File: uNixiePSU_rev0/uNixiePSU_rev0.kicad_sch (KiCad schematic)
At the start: 25 parts, among them J1 Conn_01x03, J2 Conn_01x02

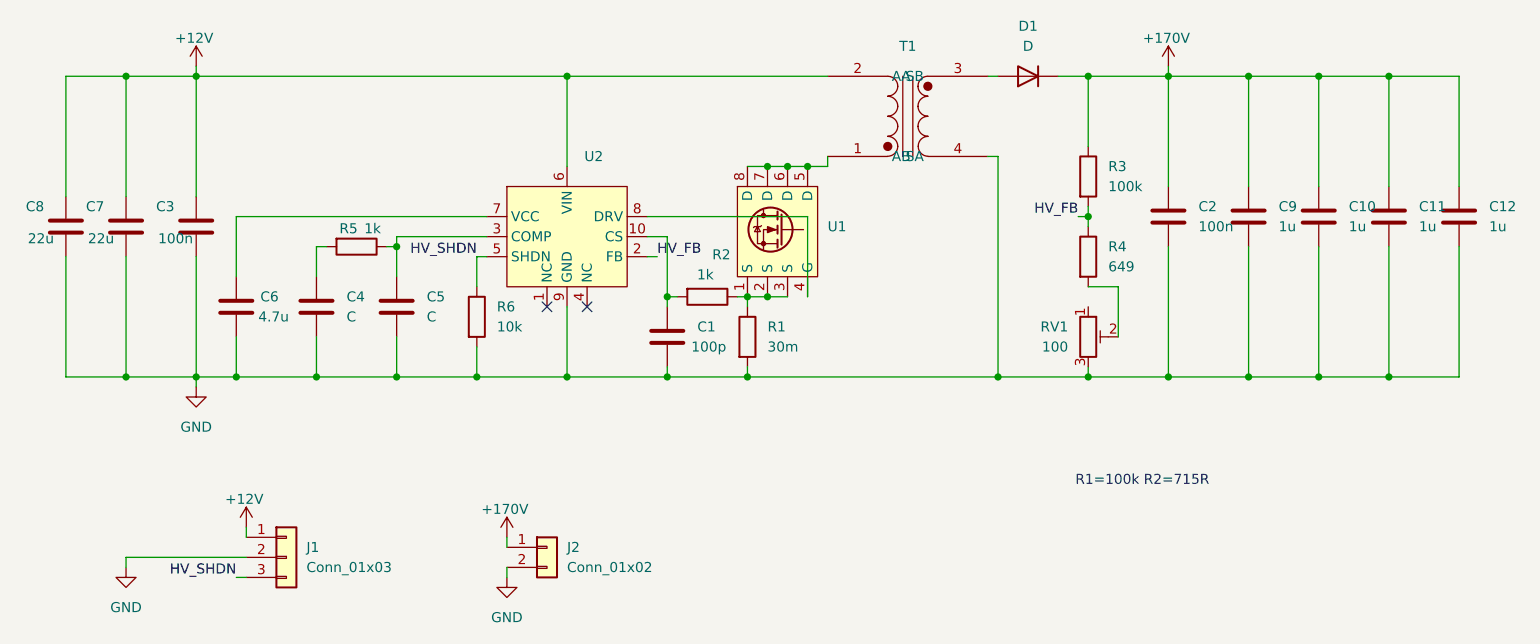
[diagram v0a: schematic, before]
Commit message: Cleanup rev0 schematic
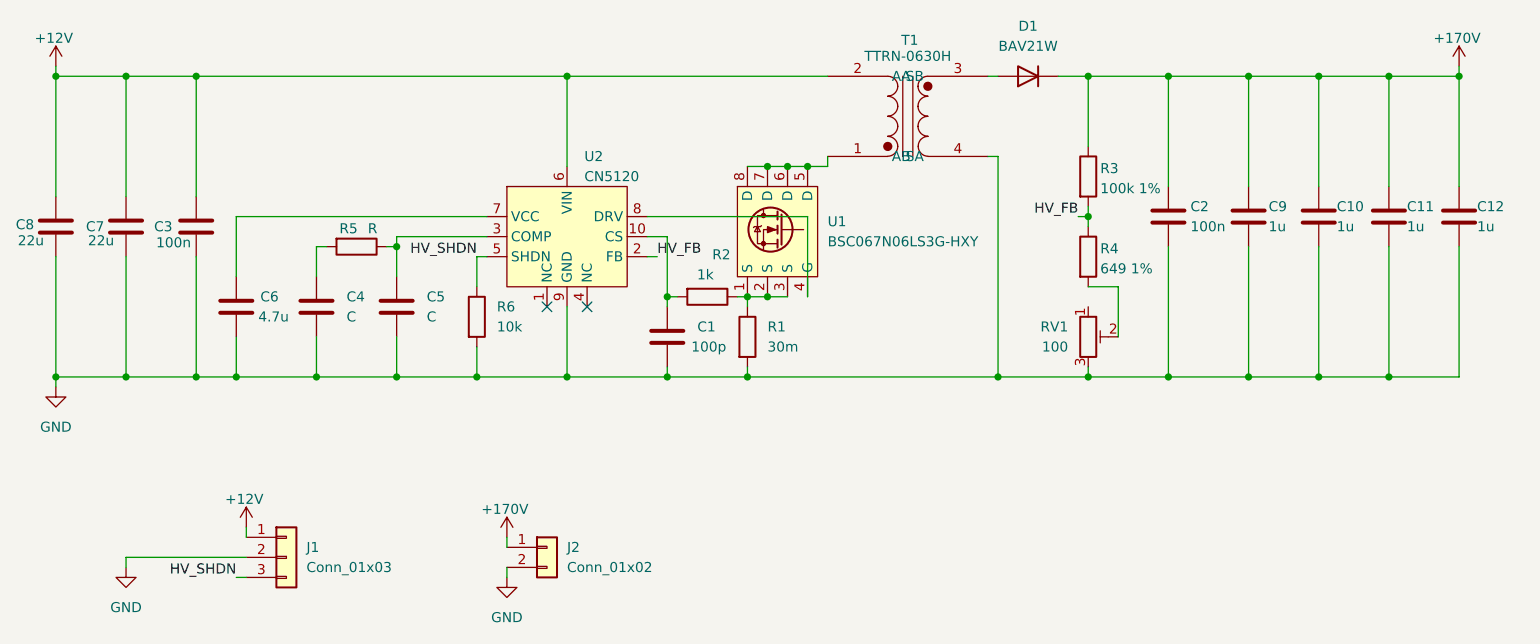
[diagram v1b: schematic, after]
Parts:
- C1: LCSC (none) -> C5186766
- C10, C11, C12, C9: LCSC (none) -> C840322
- C2, C3: LCSC (none) -> C7503480
- C6: LCSC (none) -> C6119855
- C7, C8: LCSC (none) -> C6119898
- D1: value D -> BAV21W; LCSC (none) -> C3011088
- R1: LCSC (none) -> C375524
- R2: LCSC (none) -> C2907113
- R3: value 100k -> 100k 1%; LCSC (none) -> C2907217
- R4: value 649 -> 649 1%; LCSC (none) -> C7467456
- R5: value 1k -> R
- R6: LCSC (none) -> C15401
- RV1: LCSC (none) -> C913246
- T1: value ~ -> TTRN-0630H
- U1: value ~ -> BSC067N06LS3G-HXY; LCSC (none) -> C7543016
- U2: value ~ -> CN5120; LCSC (none) -> C128237
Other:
- note removed: "R1=100k R2=715R"
- company: (none) -> Riccardo Iacob, Arwid Vasilev
- title: (none) -> uNixiePSU
- moved on the sheet: C8
